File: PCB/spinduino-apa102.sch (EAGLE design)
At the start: 31 parts, among them U1 MC74VHC1GT125DF, U2 MC74VHC1GT125DF

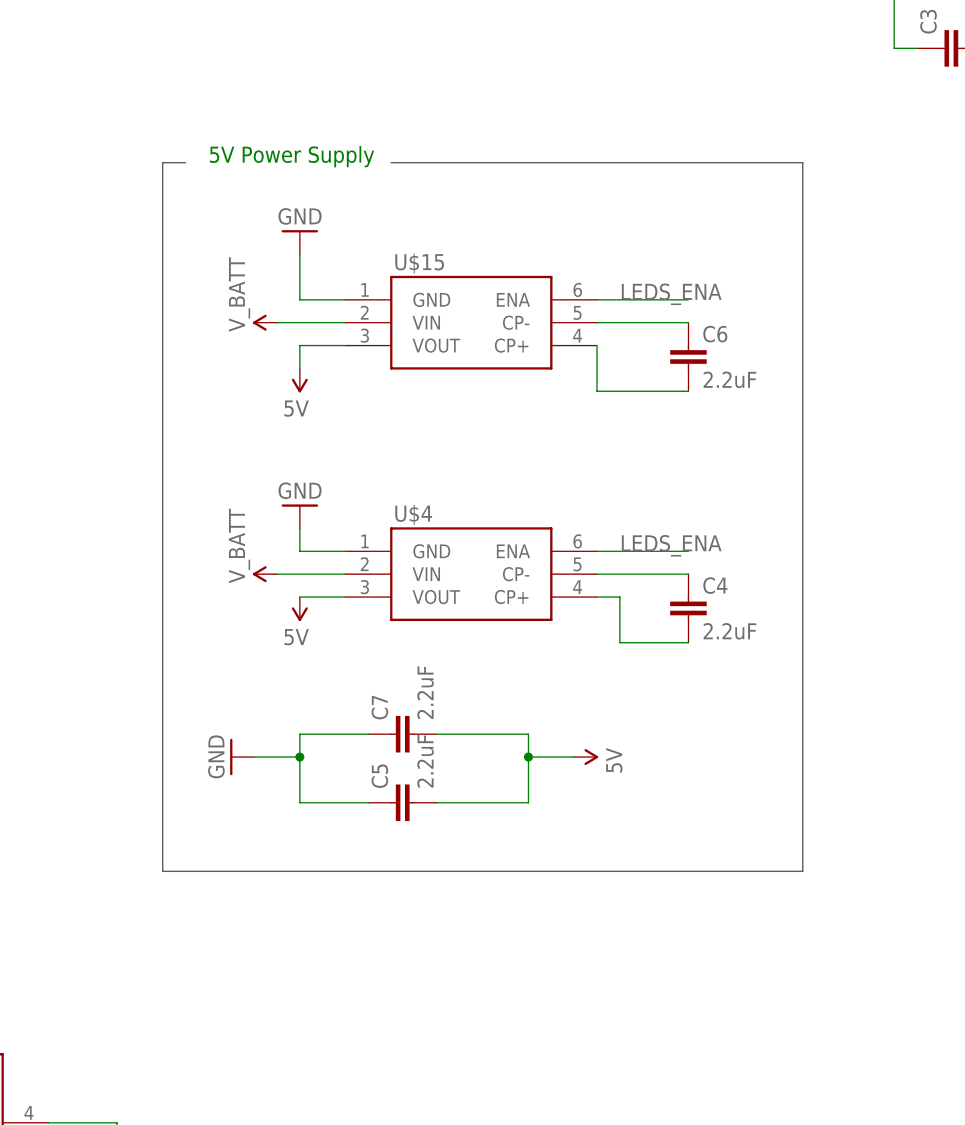
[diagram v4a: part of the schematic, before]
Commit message: fix: add pull-down resistor for the TPS60150 enable pin
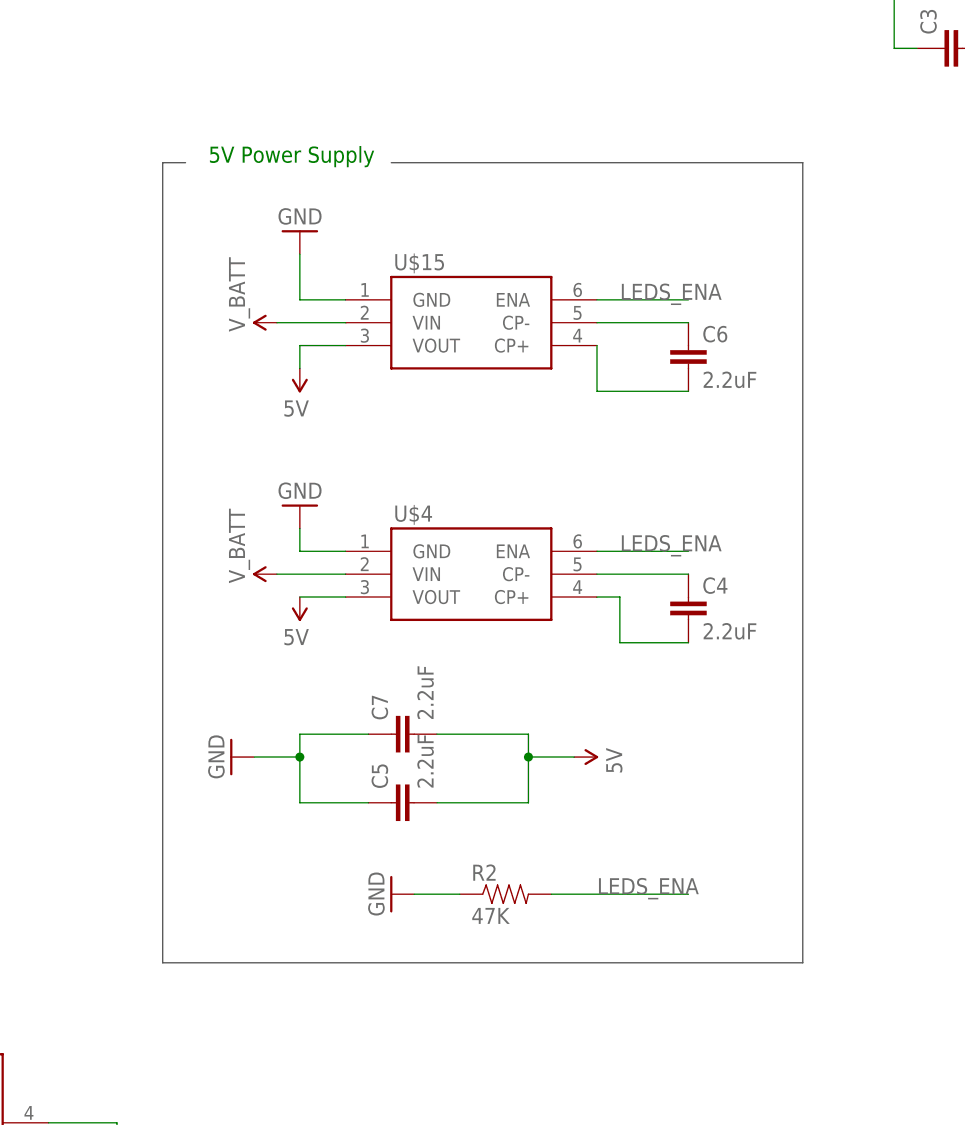
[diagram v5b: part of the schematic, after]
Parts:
- added R2: 47K, SparkFun-Resistors:1KOHM-1/10W-1%(0603)
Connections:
- net GND: now also R2.1
- net LEDS_ENA: now also R2.2
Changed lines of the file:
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@@
 <grid distance="0.1" unitdist="inch" unit="inch" style="lines" multiple="1" display="no" altdistance="0.01" altunitdist="inch" altunit="inch"/>
 <layers>
-<layer number="1" name="Top" color="4" fill="1" visible="yes" active="no"/>
-<layer number="16" name="Bottom" color="1" fill="1" visible="yes" active="no"/>
-<layer number="17" name="Pads" color="2" fill="1" visible="yes" active="no"/>
-<layer number="18" name="Vias" color="2" fill="1" visible="yes" active="no"/>
-<layer number="19" name="Unrouted" color="6" fill="1" visible="yes" active="no"/>
-<layer number="20" name="Dimension" color="15" fill="1" visible="yes" active="no"/>
-<layer number="21" name="tPlace" color="7" fill="1" visible="yes" active="no"/>
-<layer number="22" name="bPlace" color="7" fill="1" visible="yes" active="no"/>
-<layer number="23" name="tOrigins" color="15" fill="1" visible="yes" active="no"/>
-<layer number="24" name="bOrigins" color="15" fill="1" visible="yes" active="no"/>
-<layer number="25" name="tNames" color="7" fill="1" visible="yes" active="no"/>
-<layer number="26" name="bNames" color="7" fill="1" visible="yes" active="no"/>
-<layer number="27" name="tValues" color="7" fill="1" visible="yes" active="no"/>
-<layer number="28" name="bValues" color="7" fill="1" visible="yes" active="no"/>
+<layer number="1" name="Top" color="4" fill="1" visible="no" active="no"/>
+<layer number="16" name="Bottom" color="1" fill="1" visible="no" active="no"/>
+<layer number="17" name="Pads" color="2" fill="1" visible="no" active="no"/>
+<layer number="18" name="Vias" color="2" fill="1" visible="no" active="no"/>
+<layer number="19" name="Unrouted" color="6" fill="1" visible="no" active="no"/>
+<layer number="20" name="Dimension" color="15" fill="1" visible="no" active="no"/>
+<layer number="21" name="tPlace" color="7" fill="1" visible="no" active="no"/>
+<layer number="22" name="bPlace" color="7" fill="1" visible="no" active="no"/>
+<layer number="23" name="tOrigins" color="15" fill="1" visible="no" active="no"/>
+<layer number="24" name="bOrigins" color="15" fill="1" visible="no" active="no"/>
+<layer number="25" name="tNames" color="7" fill="1" visible="no" active="no"/>
+<layer number="26" name="bNames" color="7" fill="1" visible="no" active="no"/>
+<layer number="27" name="tValues" color="7" fill="1" visible="no" active="no"/>
+<layer number="28" name="bValues" color="7" fill="1" visible="no" active="no"/>
 <layer number="29" name="tStop" color="7" fill="3" visible="no" active="no"/>
 <layer number="30" name="bStop" color="7" fill="6" visible="no" active="no"/>
@@
 <layer number="35" name="tGlue" color="7" fill="4" visible="no" active="no"/>
 <layer number="36" name="bGlue" color="7" fill="5" visible="no" active="no"/>
-<layer number="37" name="tTest" color="7" fill="1" visible="yes" active="no"/>
-<layer number="38" name="bTest" color="7" fill="1" visible="yes" active="no"/>
+<layer number="37" name="tTest" color="7" fill="1" visible="no" active="no"/>
+<layer number="38" name="bTest" color="7" fill="1" visible="no" active="no"/>
 <layer number="39" name="tKeepout" color="4" fill="11" visible="no" active="no"/>
 <layer number="40" name="bKeepout" color="1" fill="11" visible="no" active="no"/>
@@
 <layer number="44" name="Drills" color="7" fill="1" visible="no" active="no"/>
 <layer number="45" name="Holes" color="7" fill="1" visible="no" active="no"/>
-<layer number="46" name="Milling" color="3" fill="1" visible="yes" active="no"/>
-<layer number="47" name="Measures" color="7" fill="1" visible="yes" active="no"/>
-<layer number="48" name="Document" color="7" fill="1" visible="yes" active="no"/>
-<layer number="49" name="Reference" color="7" fill="1" visible="yes" active="no"/>
-<layer number="50" name="dxf" color="7" fill="1" visible="yes" active="no"/>
-<layer number="51" name="tDocu" color="7" fill="1" visible="yes" active="no"/>
-<layer number="52" name="bDocu" color="7" fill="1" visible="yes" active="no"/>
-<layer number="53" name="tGND_GNDA" color="7" fill="1" visible="yes" active="no"/>
-<layer number="54" name="bGND_GNDA" color="7" fill="1" visible="yes" active="no"/>
-<layer number="56" name="wert" color="7" fill="1" visible="yes" active="no"/>
-<layer number="57" name="tCAD" color="7" fill="1" visible="yes" active="no"/>
-<layer number="59" name="tCarbon" color="7" fill="1" visible="yes" active="no"/>
-<layer number="60" name="bCarbon" color="7" fill="1" visible="yes" active="no"/>
+<layer number="46" name="Milling" color="3" fill="1" visible="no" active="no"/>
+<layer number="47" name="Measures" color="7" fill="1" visible="no" active="no"/>
+<layer number="48" name="Document" color="7" fill="1" visible="no" active="no"/>
+<layer number="49" name="Reference" color="7" fill="1" visible="no" active="no"/>
+<layer number="50" name="dxf" color="7" fill="1" visible="no" active="no"/>
+<layer number="51" name="tDocu" color="7" fill="1" visible="no" active="no"/>
+<layer number="52" name="bDocu" color="7" fill="1" visible="no" active="no"/>
+<layer number="53" name="tGND_GNDA" color="7" fill="1" visible="no" active="no"/>
+<layer number="54" name="bGND_GNDA" color="7" fill="1" visible="no" active="no"/>
+<layer number="56" name="wert" color="7" fill="1" visible="no" active="no"/>
+<layer number="57" name="tCAD" color="7" fill="1" visible="no" active="no"/>
+<layer number="59" name="tCarbon" color="7" fill="1" visible="no" active="no"/>
+<layer number="60" name="bCarbon" color="7" fill="1" visible="no" active="no"/>
 <layer number="90" name="Modules" color="5" fill="1" visible="yes" active="yes"/>
 <layer number="91" name="Nets" color="2" fill="1" visible="yes" active="yes"/>
@@
 <part name="C6" library="SparkFun-Capacitors" deviceset="2.2UF-10V-20%(0603)" device="" value="2.2uF"/>
 <part name="C7" library="SparkFun-Capacitors" deviceset="10UF-6.3V-20%(0603)" device="" value="2.2uF"/>
+<part name="R2" library="SparkFun-Resistors" deviceset="1KOHM-1/10W-1%(0603)" device="" value="47K"/>
+<part name="GND19" library="ng-beacon" deviceset="GND" device=""/>
 </parts>
 <sheets>
@@
 <text x="-50.8" y="91.44" size="1.778" layer="91">5V Power Supply</text>
 <wire x1="-53.34" y1="91.44" x2="-55.88" y2="91.44" width="0.1524" layer="97"/>
-<wire x1="-55.88" y1="91.44" x2="-55.88" y2="12.7" width="0.1524" layer="97"/>
-<wire x1="-55.88" y1="12.7" x2="15.24" y2="12.7" width="0.1524" layer="97"/>
-<wire x1="15.24" y1="12.7" x2="15.24" y2="91.44" width="0.1524" layer="97"/>
+<wire x1="-55.88" y1="91.44" x2="-55.88" y2="2.54" width="0.1524" layer="97"/>
+<wire x1="-55.88" y1="2.54" x2="15.24" y2="2.54" width="0.1524" layer="97"/>
+<wire x1="15.24" y1="2.54" x2="15.24" y2="91.44" width="0.1524" layer="97"/>
 <wire x1="15.24" y1="91.44" x2="-30.48" y2="91.44" width="0.1524" layer="97"/>
 </plain>
@@
 <instance part="C6" gate="G$1" x="2.54" y="68.58"/>
 <instance part="C7" gate="G$1" x="-27.94" y="27.94" rot="R90"/>
+<instance part="R2" gate="G$1" x="-17.78" y="10.16"/>
+<instance part="GND19" gate="1" x="-30.48" y="10.16" rot="R270"/>
 </instances>
 <busses>
@@
 <junction x="-40.64" y="25.4"/>
 </segment>
+<segment>
+<pinref part="R2" gate="G$1" pin="1"/>
+<pinref part="GND19" gate="1" pin="GND"/>
+<wire x1="-22.86" y1="10.16" x2="-27.94" y2="10.16" width="0.1524" layer="91"/>
+</segment>
 </net>
 <net name="HALL1" class="0">
@@
 <label x="69.342" y="25.4" size="1.778" layer="95" rot="R270"/>
 </segment>
-</net>
+<segment>
+<wire x1="-12.7" y1="10.16" x2="2.54" y2="10.16" width="0.1524" layer="91"/>
+<label x="-7.62" y="10.16" size="1.778" layer="95"/>
+<pinref part="R2" gate="G$1" pin="2"/>
+</segment>
+</net>

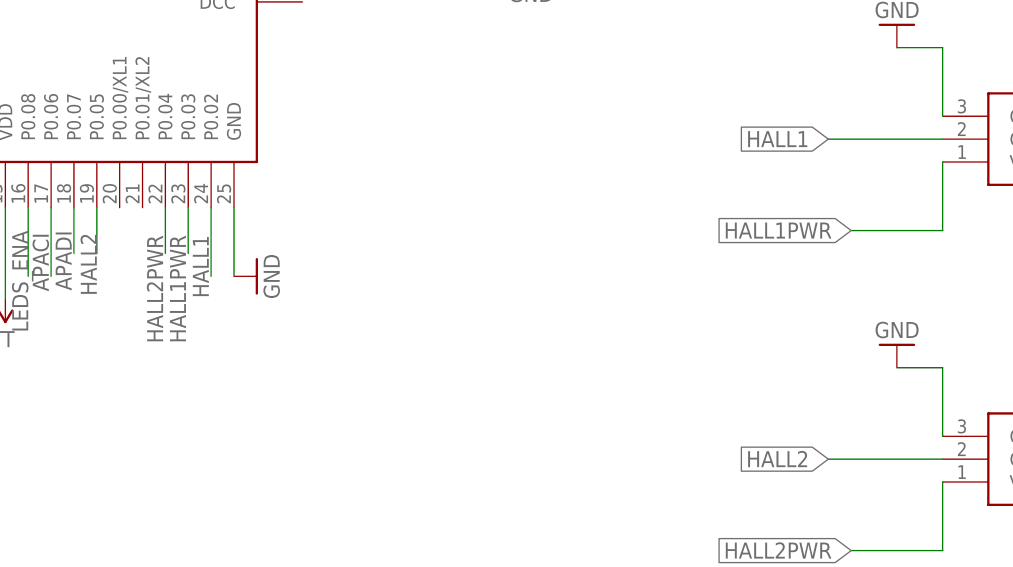
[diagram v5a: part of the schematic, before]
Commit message: fix: connect one of the hall effect sensors to the 5v power supply
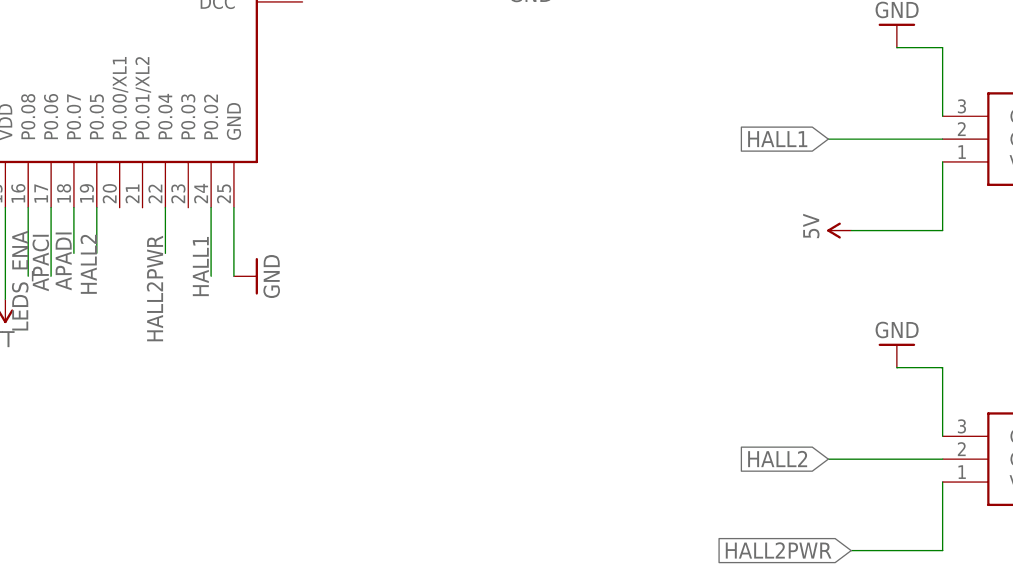
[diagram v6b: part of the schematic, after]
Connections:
- removed net HALL1PWR: U$1.P0.03, U$2.VS
- net 5V: now also U$2.VS
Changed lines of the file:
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@@
 <part name="R2" library="SparkFun-Resistors" deviceset="1KOHM-1/10W-1%(0603)" device="" value="47K"/>
 <part name="GND19" library="ng-beacon" deviceset="GND" device=""/>
+<part name="SUPPLY16" library="SparkFun-Aesthetics" deviceset="5V" device=""/>
 </parts>
 <sheets>
@@
 <instance part="R2" gate="G$1" x="-17.78" y="10.16"/>
 <instance part="GND19" gate="1" x="-30.48" y="10.16" rot="R270"/>
+<instance part="SUPPLY16" gate="G$1" x="162.56" y="25.4" rot="R90"/>
 </instances>
 <busses>
@@
 </segment>
 </net>
-<net name="HALL1PWR" class="0">
-<segment>
-<wire x1="172.72" y1="33.02" x2="172.72" y2="25.4" width="0.1524" layer="91"/>
-<pinref part="U$2" gate="G$1" pin="VS"/>
-<wire x1="172.72" y1="25.4" x2="162.56" y2="25.4" width="0.1524" layer="91"/>
-<label x="162.56" y="25.4" size="1.778" layer="95" rot="R180" xref="yes"/>
-</segment>
-<segment>
-<pinref part="U$1" gate="G$1" pin="P0.03"/>
-<wire x1="88.9" y1="27.94" x2="88.9" y2="22.86" width="0.1524" layer="91"/>
-<label x="86.868" y="24.892" size="1.778" layer="95" rot="R270"/>
-</segment>
-</net>
 <net name="HALL2PWR" class="0">
 <segment>
@@
 <junction x="-15.24" y="25.4"/>
 </segment>
-</net>
+<segment>
+<wire x1="172.72" y1="33.02" x2="172.72" y2="25.4" width="0.1524" layer="91"/>
+<pinref part="U$2" gate="G$1" pin="VS"/>
+<wire x1="172.72" y1="25.4" x2="162.56" y2="25.4" width="0.1524" layer="91"/>
+<pinref part="SUPPLY16" gate="G$1" pin="5V"/>
+</segment>
+</net>
